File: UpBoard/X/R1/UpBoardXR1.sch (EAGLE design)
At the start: 63 parts, among them CN1 100nF, CN2 100nF, CN3 100nF, CN4 100nF, IC1 SAM3X8E(ARDUINO), IC2 W25N01GVZEIG/IT, Q2 MBT3904DW2T1, X1 16POS_RIBBON, X2 16POS_RIBBON, X3 16POS_RIBBON, X4 16POS_RIBBON, Y1 FH1200001, Y2 ABS05

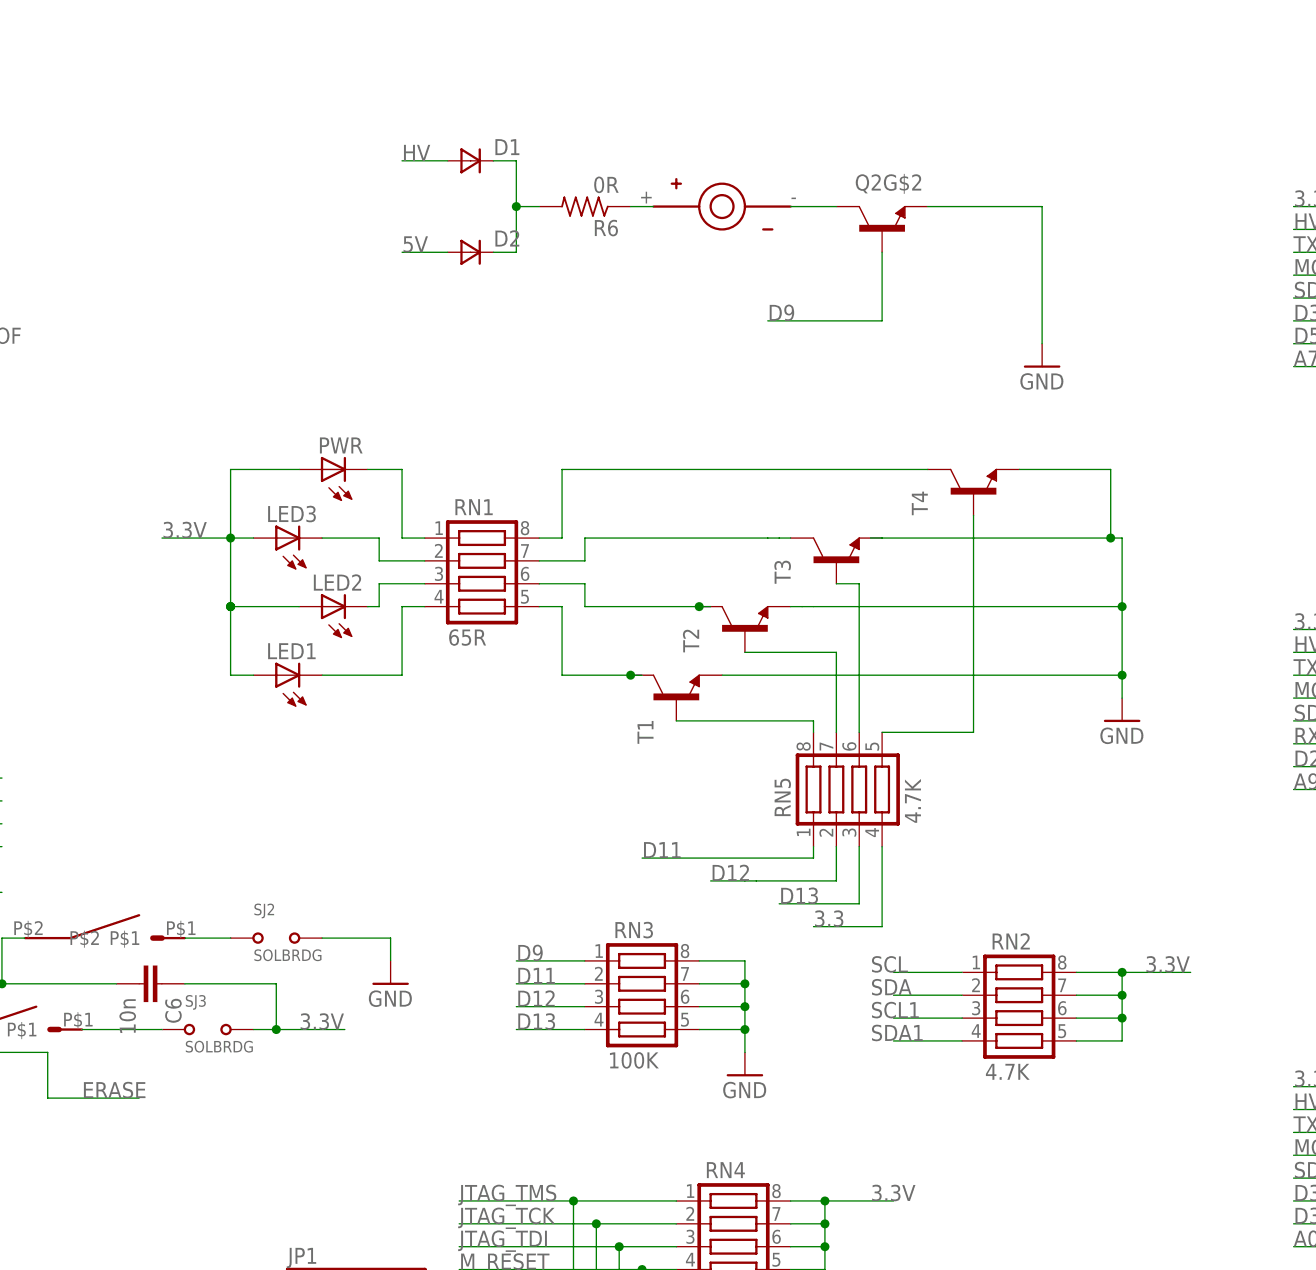
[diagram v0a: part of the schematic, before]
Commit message: Added in and routed bjt arrays
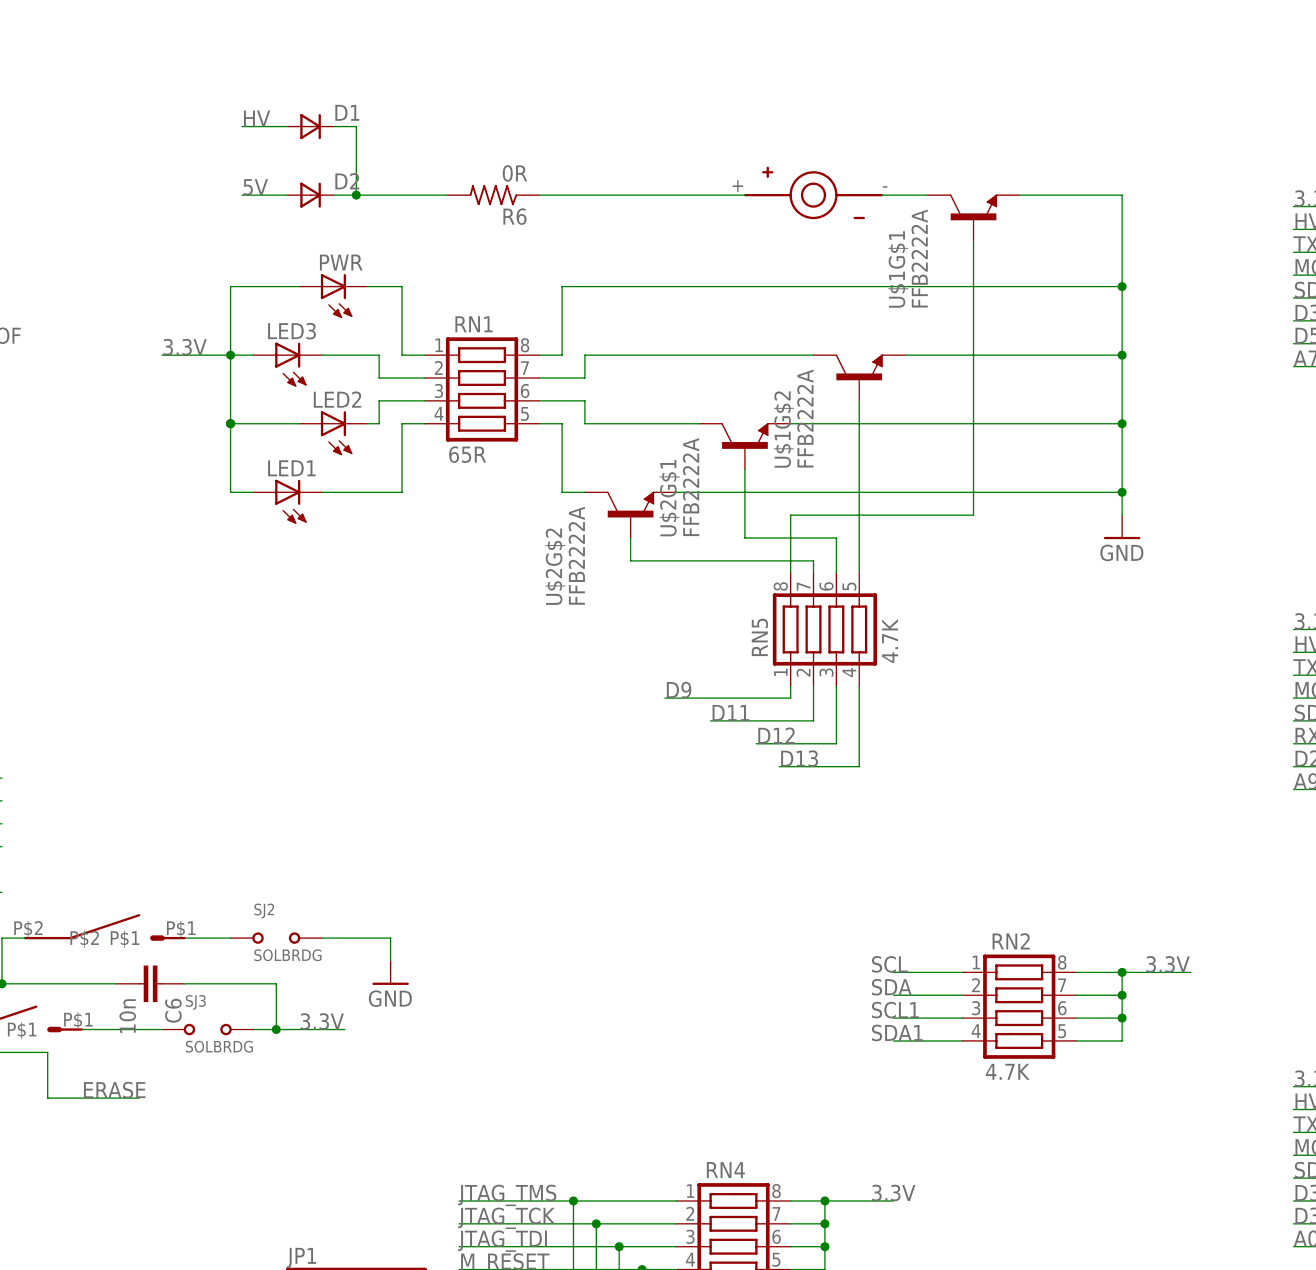
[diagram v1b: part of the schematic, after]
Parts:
- removed Q2: MBT3904DW2T1, CPSS_IC:MBT3904DW2T1
- removed RN3: 100K, resistor-net:CTS742C083
- removed T1, T2, T3, T4: (no value), transistor:BC808-NPN-SOT23-BEC
- added U$1, U$2: FFB2222A, CPSS_IC:FFB2222A
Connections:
- removed net 3.3: RN5.4
- removed net N$18: RN5.6, T3.B
- net D11: now also RN5.2; no longer RN3.2, RN5.1
- net D12: now also RN5.3; no longer RN3.3, RN5.2
- net D13: now also RN5.4; no longer RN3.4, RN5.3
- net D9: now also RN5.1; no longer Q2G$2.B, RN3.1
- net GND: now also RN1.8, U$1G$1.E, U$1G$2.E, U$2G$1.E, U$2G$2.E; no longer Q2G$2.E, RN3.5, RN3.6, RN3.7, RN3.8, T1.E, T2.E, T3.E, T4.E
- net N$10: now also U$1G$2.C; no longer T3.C
- net N$11: now also U$2G$1.C; no longer T2.C
- net N$12: now also U$2G$2.C; no longer T1.C
- net N$16: now also RN5.6, U$2G$1.B; no longer RN5.8, T1.B
- net N$17: now also U$2G$2.B; no longer T2.B
- net N$19: now also RN5.8, U$1G$1.B; no longer RN5.5, T4.B
- net N$33: now also U$1G$1.C; no longer Q2G$2.C
- net N$8: now also RN5.5, U$1G$2.B; no longer RN1.8, T4.C
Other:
- moved on the sheet: D1, D2, LED1, LED2, LED3, PWR, R6, RN1, RN5

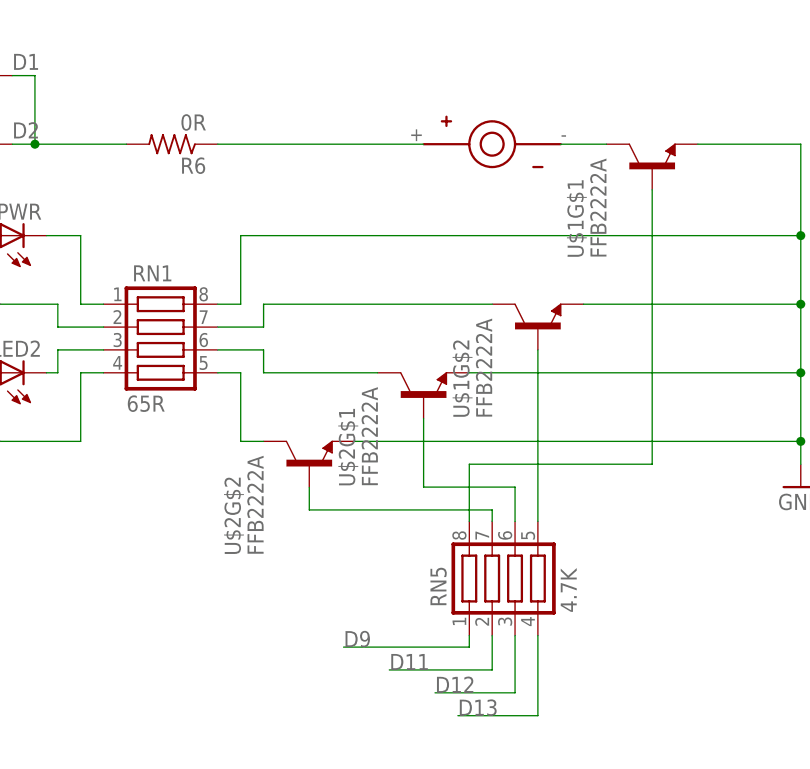
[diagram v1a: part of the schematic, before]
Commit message: Fixed naming and silkscreen
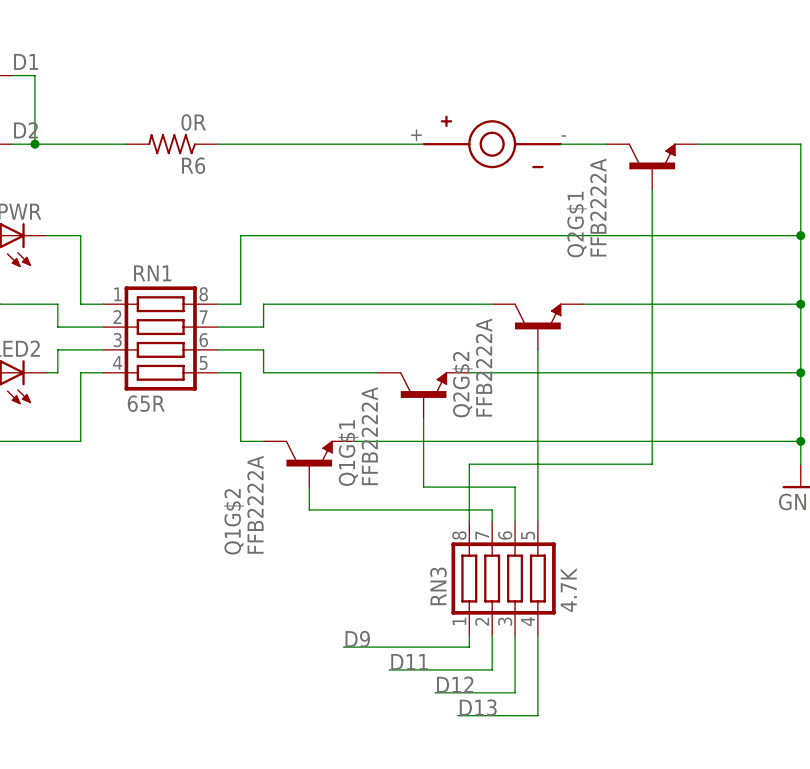
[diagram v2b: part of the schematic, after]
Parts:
- renumbered RN5 to RN3, U$1 to Q2, U$2 to Q1
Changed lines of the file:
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@@
 <part name="SJ3" library="CPSS_CONNECTOR" deviceset="SOLBRDG" device=""/>
 <part name="SJ2" library="CPSS_CONNECTOR" deviceset="SOLBRDG" device=""/>
-<part name="RN5" library="resistor-net" library_urn="urn:adsk.eagle:library:343" deviceset="CTS742C083" device="" package3d_urn="urn:adsk.eagle:package:24985/1" value="4.7K"/>
-<part name="U$1" library="CPSS_IC" deviceset="FFB2222A" device=""/>
-<part name="U$2" library="CPSS_IC" deviceset="FFB2222A" device=""/>
+<part name="RN3" library="resistor-net" library_urn="urn:adsk.eagle:library:343" deviceset="CTS742C083" device="" package3d_urn="urn:adsk.eagle:package:24985/1" value="4.7K"/>
+<part name="Q2" library="CPSS_IC" deviceset="FFB2222A" device=""/>
+<part name="Q1" library="CPSS_IC" deviceset="FFB2222A" device=""/>
 </parts>
 <sheets>
@@
 <instance part="SJ3" gate="G$1" x="262.89" y="158.75"/>
 <instance part="SJ2" gate="G$1" x="270.51" y="168.91"/>
-<instance part="RN5" gate="G$1" x="330.2" y="201.93" rot="R90"/>
-<instance part="U$1" gate="G$1" x="347.98" y="248.92" rot="R90"/>
-<instance part="U$1" gate="G$2" x="335.28" y="231.14" rot="R90"/>
-<instance part="U$2" gate="G$1" x="322.58" y="223.52" rot="R90"/>
-<instance part="U$2" gate="G$2" x="309.88" y="215.9" rot="R90"/>
+<instance part="RN3" gate="G$1" x="330.2" y="201.93" rot="R90"/>
+<instance part="Q2" gate="G$1" x="347.98" y="248.92" rot="R90"/>
+<instance part="Q2" gate="G$2" x="335.28" y="231.14" rot="R90"/>
+<instance part="Q1" gate="G$1" x="322.58" y="223.52" rot="R90"/>
+<instance part="Q1" gate="G$2" x="309.88" y="215.9" rot="R90"/>
 </instances>
 <busses>
@@
 <label x="313.69" y="195.58" size="1.778" layer="95"/>
 <wire x1="327.66" y1="195.58" x2="313.69" y2="195.58" width="0.1524" layer="91"/>
-<pinref part="RN5" gate="G$1" pin="1"/>
+<pinref part="RN3" gate="G$1" pin="1"/>
 <wire x1="327.66" y1="195.58" x2="327.66" y2="196.85" width="0.1524" layer="91"/>
 </segment>
@@
 <junction x="364.49" y="218.44"/>
 <pinref part="GND3" gate="1" pin="GND"/>
-<pinref part="U$1" gate="G$2" pin="E"/>
-<pinref part="U$2" gate="G$1" pin="E"/>
-<pinref part="U$2" gate="G$2" pin="E"/>
+<pinref part="Q2" gate="G$2" pin="E"/>
+<pinref part="Q1" gate="G$1" pin="E"/>
+<pinref part="Q1" gate="G$2" pin="E"/>
 <wire x1="353.06" y1="251.46" x2="364.49" y2="251.46" width="0.1524" layer="91"/>
 <wire x1="364.49" y1="251.46" x2="364.49" y2="241.3" width="0.1524" layer="91"/>
@@
 <wire x1="302.26" y1="241.3" x2="364.49" y2="241.3" width="0.1524" layer="91"/>
 <junction x="364.49" y="241.3"/>
-<pinref part="U$1" gate="G$1" pin="E"/>
+<pinref part="Q2" gate="G$1" pin="E"/>
 </segment>
 <segment>
@@
 <label x="326.39" y="187.96" size="1.778" layer="95"/>
 <wire x1="326.39" y1="187.96" x2="335.28" y2="187.96" width="0.1524" layer="91"/>
-<pinref part="RN5" gate="G$1" pin="4"/>
+<pinref part="RN3" gate="G$1" pin="4"/>
 <wire x1="335.28" y1="187.96" x2="335.28" y2="196.85" width="0.1524" layer="91"/>
 </segment>
@@
 <wire x1="342.9" y1="251.46" x2="337.82" y2="251.46" width="0.1524" layer="91"/>
 <pinref part="LS1" gate="G$1" pin="-"/>
-<pinref part="U$1" gate="G$1" pin="C"/>
+<pinref part="Q2" gate="G$1" pin="C"/>
 </segment>
 </net>
@@
 <label x="318.77" y="193.04" size="1.778" layer="95"/>
 <wire x1="318.77" y1="193.04" x2="330.2" y2="193.04" width="0.1524" layer="91"/>
-<pinref part="RN5" gate="G$1" pin="2"/>
+<pinref part="RN3" gate="G$1" pin="2"/>
 <wire x1="330.2" y1="193.04" x2="330.2" y2="196.85" width="0.1524" layer="91"/>
 </segment>
@@
 <label x="323.85" y="190.5" size="1.778" layer="95"/>
 <wire x1="332.74" y1="190.5" x2="323.85" y2="190.5" width="0.1524" layer="91"/>
-<pinref part="RN5" gate="G$1" pin="3"/>
+<pinref part="RN3" gate="G$1" pin="3"/>
 <wire x1="332.74" y1="190.5" x2="332.74" y2="196.85" width="0.1524" layer="91"/>
 </segment>
@@
 <pinref part="RN1" gate="G$1" pin="7"/>
 <wire x1="304.8" y1="231.14" x2="299.72" y2="231.14" width="0.1524" layer="91"/>
-<pinref part="U$1" gate="G$2" pin="C"/>
+<pinref part="Q2" gate="G$2" pin="C"/>
 </segment>
 </net>
@@
 <wire x1="304.8" y1="228.6" x2="304.8" y2="226.06" width="0.1524" layer="91"/>
 <wire x1="304.8" y1="226.06" x2="317.5" y2="226.06" width="0.1524" layer="91"/>
-<pinref part="U$2" gate="G$1" pin="C"/>
+<pinref part="Q1" gate="G$1" pin="C"/>
 </segment>
 </net>
@@
 <wire x1="302.26" y1="226.06" x2="302.26" y2="218.44" width="0.1524" layer="91"/>
 <wire x1="302.26" y1="218.44" x2="304.8" y2="218.44" width="0.1524" layer="91"/>
-<pinref part="U$2" gate="G$2" pin="C"/>
+<pinref part="Q1" gate="G$2" pin="C"/>
 </segment>
 </net>
 <net name="N$16" class="0">
 <segment>
-<pinref part="U$2" gate="G$1" pin="B"/>
+<pinref part="Q1" gate="G$1" pin="B"/>
 <wire x1="322.58" y1="220.98" x2="322.58" y2="213.36" width="0.1524" layer="91"/>
 <wire x1="322.58" y1="213.36" x2="332.74" y2="213.36" width="0.1524" layer="91"/>
-<pinref part="RN5" gate="G$1" pin="6"/>
+<pinref part="RN3" gate="G$1" pin="6"/>
 <wire x1="332.74" y1="209.55" x2="332.74" y2="213.36" width="0.1524" layer="91"/>
 </segment>
@@
 <segment>
 <wire x1="330.2" y1="210.82" x2="309.88" y2="210.82" width="0.1524" layer="91"/>
-<pinref part="U$2" gate="G$2" pin="B"/>
+<pinref part="Q1" gate="G$2" pin="B"/>
 <wire x1="309.88" y1="213.36" x2="309.88" y2="210.82" width="0.1524" layer="91"/>
-<pinref part="RN5" gate="G$1" pin="7"/>
+<pinref part="RN3" gate="G$1" pin="7"/>
 <wire x1="330.2" y1="209.55" x2="330.2" y2="210.82" width="0.1524" layer="91"/>
 </segment>
@@
 <net name="N$19" class="0">
 <segment>
-<pinref part="U$1" gate="G$1" pin="B"/>
-<pinref part="RN5" gate="G$1" pin="8"/>
+<pinref part="Q2" gate="G$1" pin="B"/>
+<pinref part="RN3" gate="G$1" pin="8"/>
 <wire x1="347.98" y1="215.9" x2="347.98" y2="246.38" width="0.1524" layer="91"/>
 <wire x1="327.66" y1="209.55" x2="327.66" y2="215.9" width="0.1524" layer="91"/>
@@
 <net name="N$8" class="0">
 <segment>
-<pinref part="RN5" gate="G$1" pin="5"/>
-<pinref part="U$1" gate="G$2" pin="B"/>
+<pinref part="RN3" gate="G$1" pin="5"/>
+<pinref part="Q2" gate="G$2" pin="B"/>
 <wire x1="335.28" y1="209.55" x2="335.28" y2="228.6" width="0.1524" layer="91"/>
 </segment>
